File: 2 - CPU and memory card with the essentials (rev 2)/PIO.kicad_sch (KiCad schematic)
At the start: 5 parts, among them J12 LPT or Keyboard, J14 PIO HEADER, U15 Z84C20xx PIO

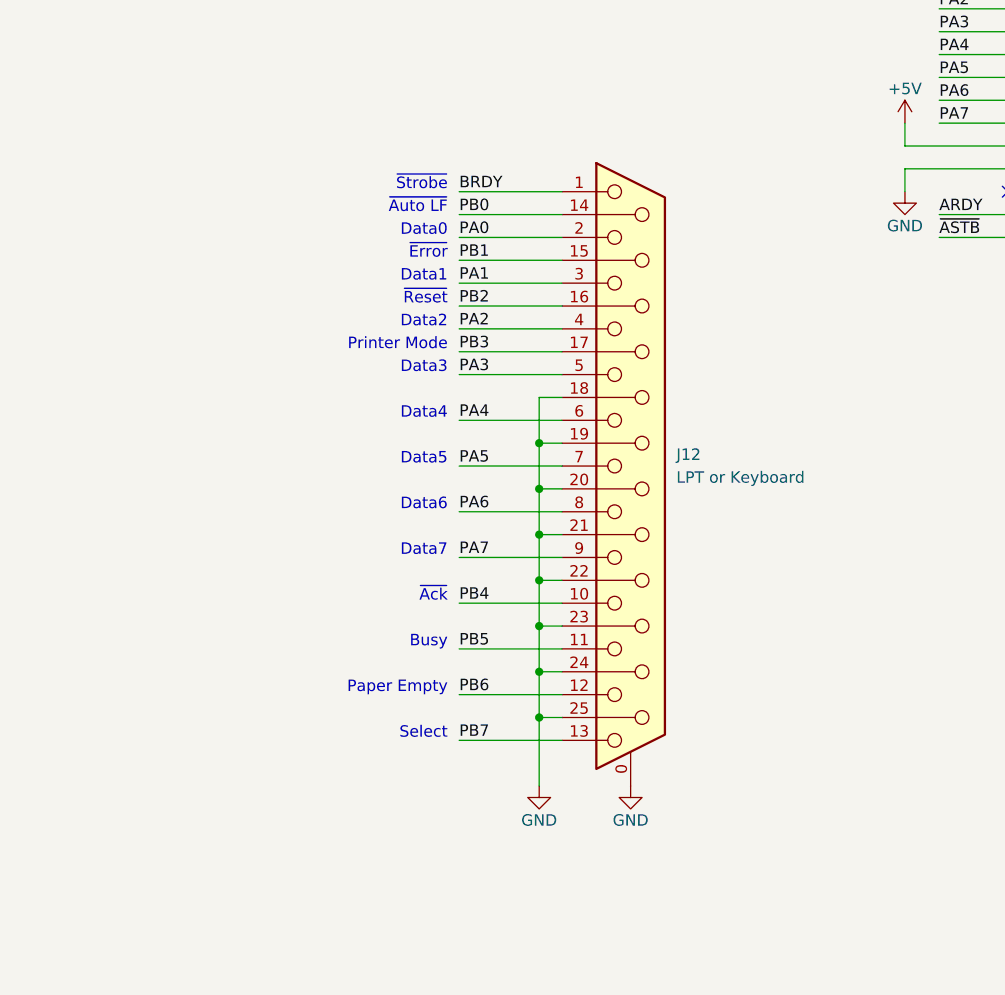
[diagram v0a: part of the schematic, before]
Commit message: Updated disk activity circuit in mother board, and improved layout in CPU card
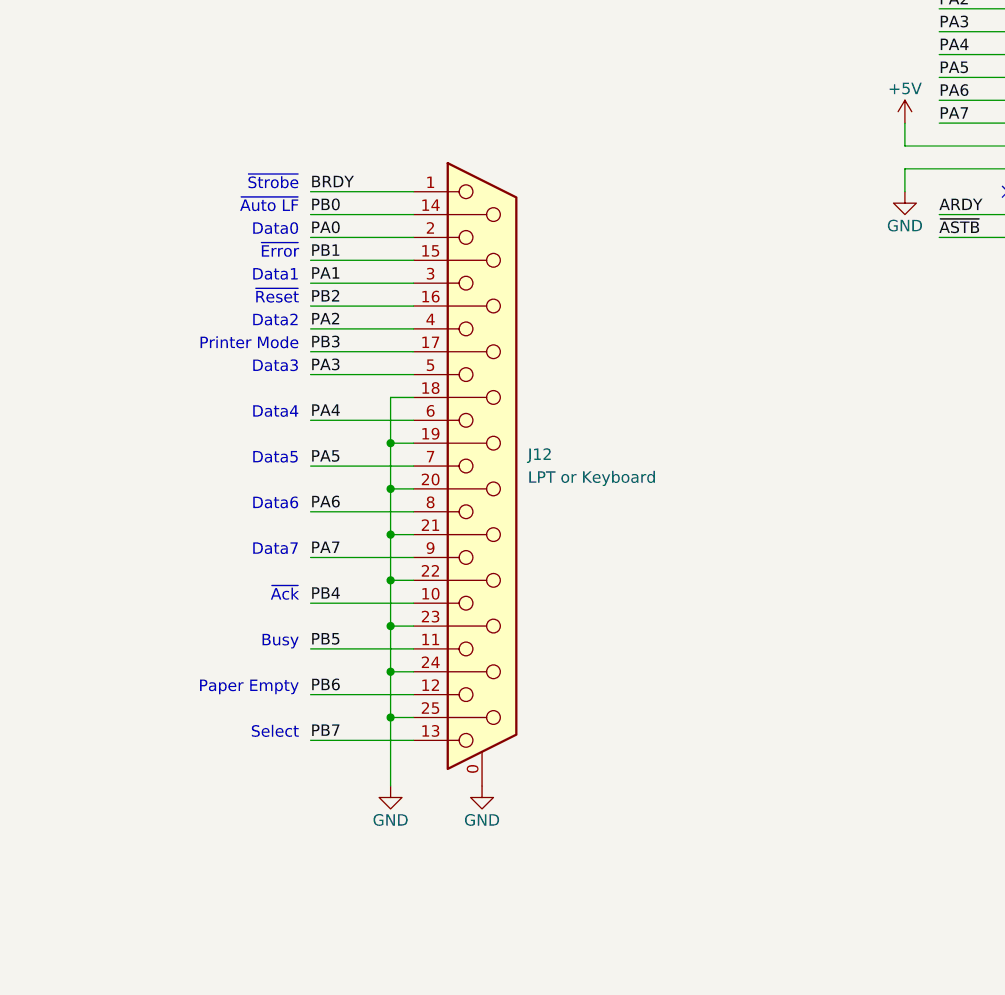
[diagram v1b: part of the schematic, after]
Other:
- moved on the sheet: J12
